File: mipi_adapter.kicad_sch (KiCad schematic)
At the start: 0 parts

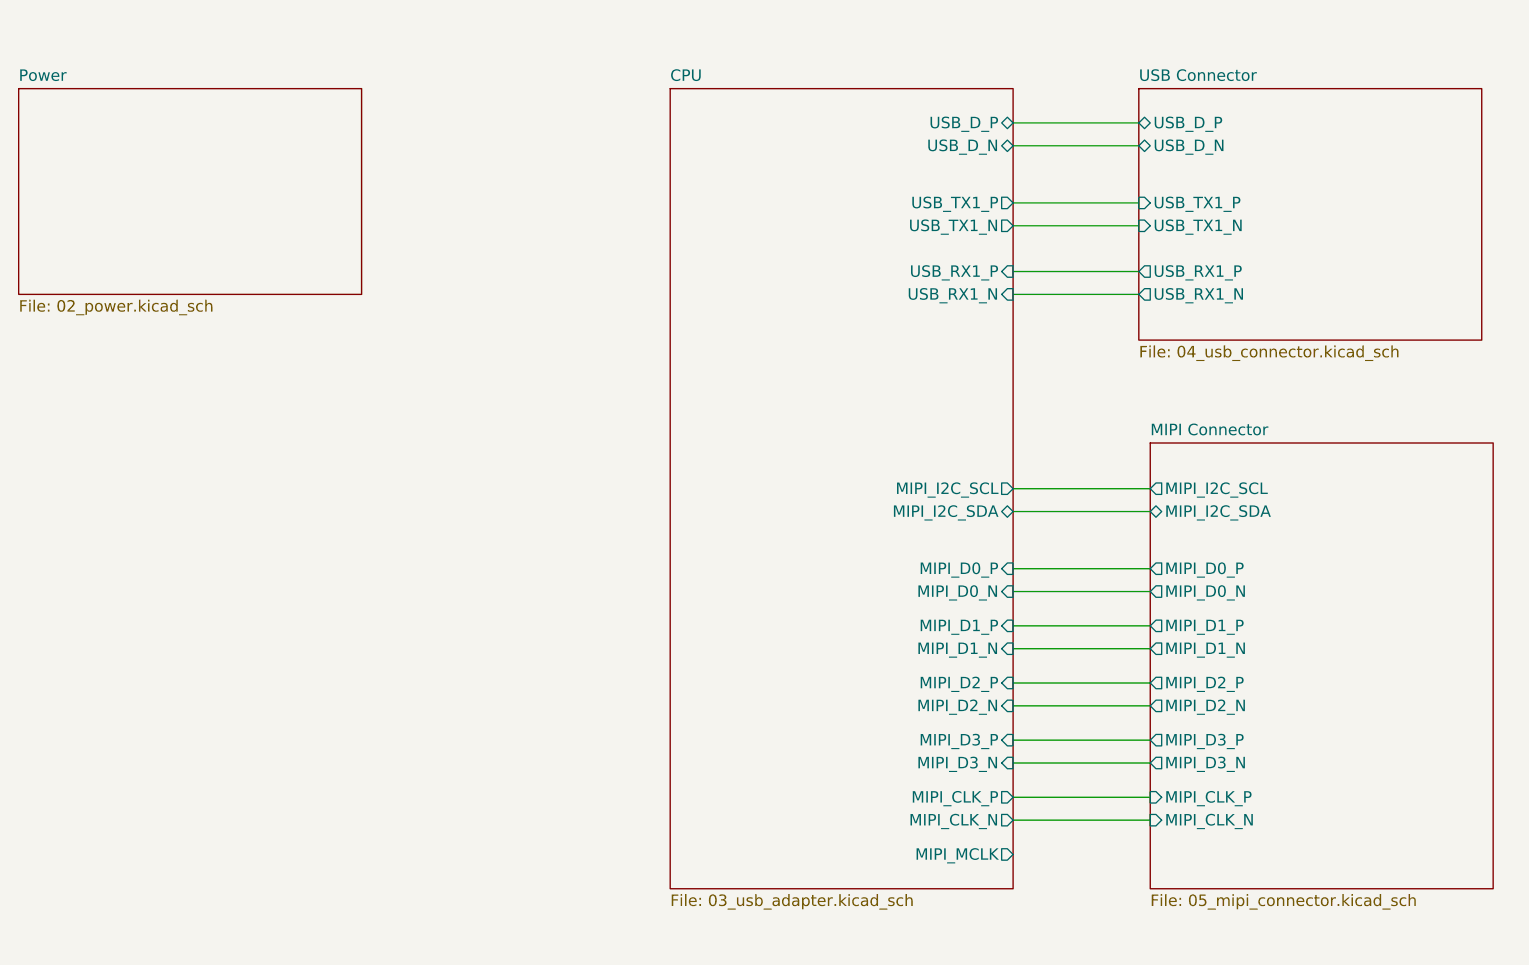
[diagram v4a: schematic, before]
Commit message: cleaned up some DRC errors
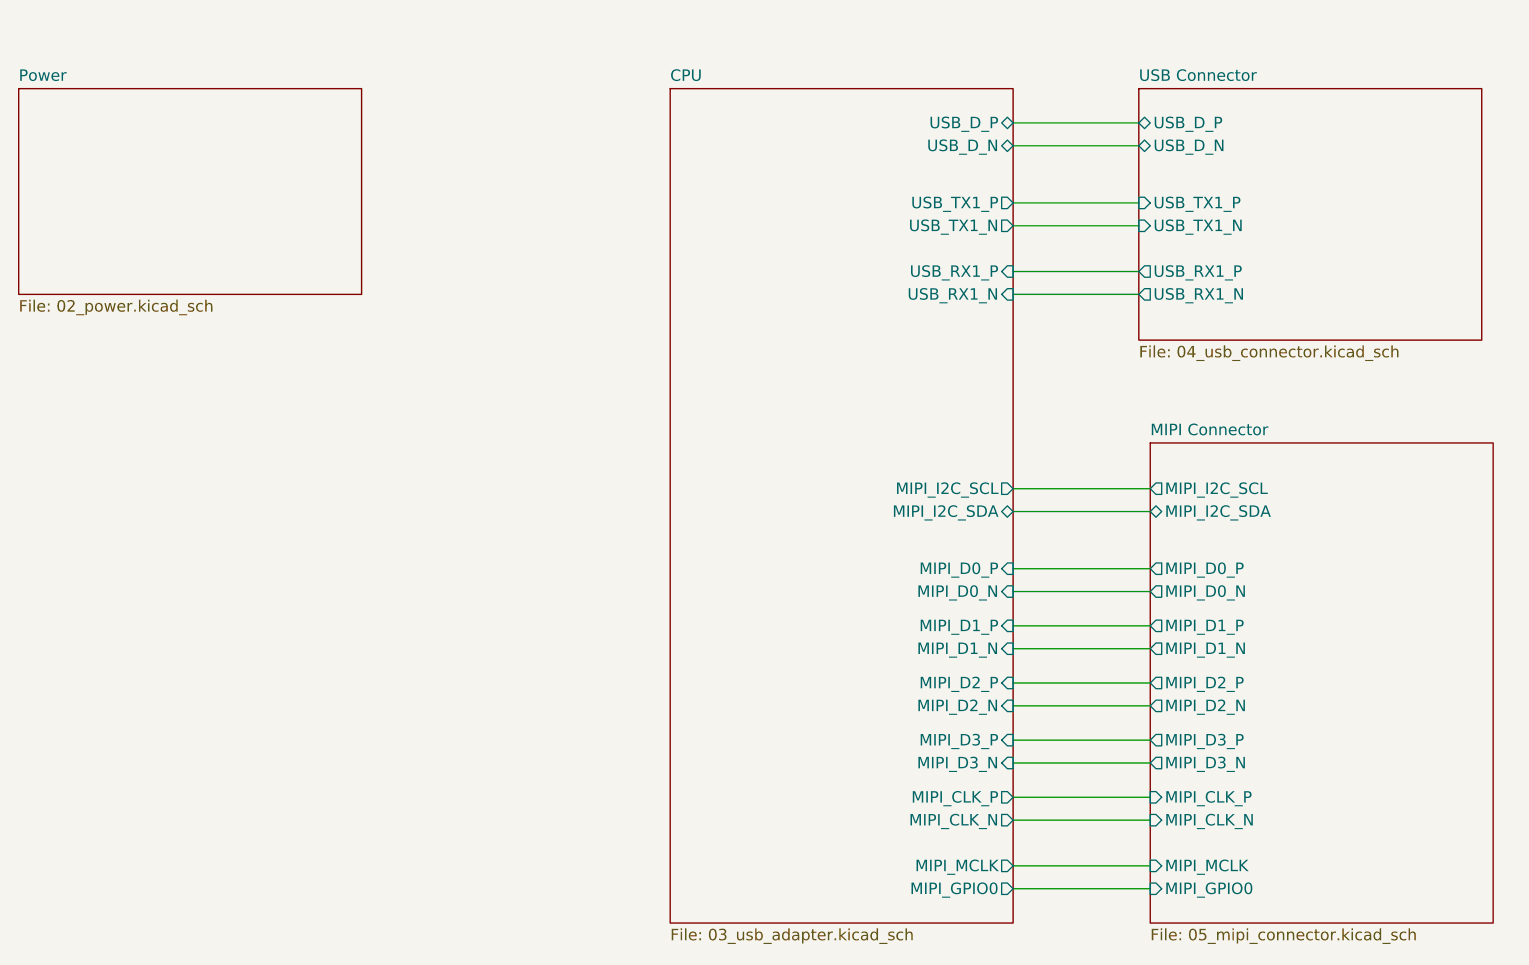
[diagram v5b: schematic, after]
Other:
- sheet CPU ports: added MIPI_GPIO0; removed none
- sheet MIPI Connector ports: added MIPI_GPIO0, MIPI_MCLK; removed none
